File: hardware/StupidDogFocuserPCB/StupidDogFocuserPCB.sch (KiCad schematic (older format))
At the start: 17 parts, among them M1 Stepper_Motor_bipolar, SW1 Rotary_Encoder_Switch, U1 DHT11, U2 SN74HC14N

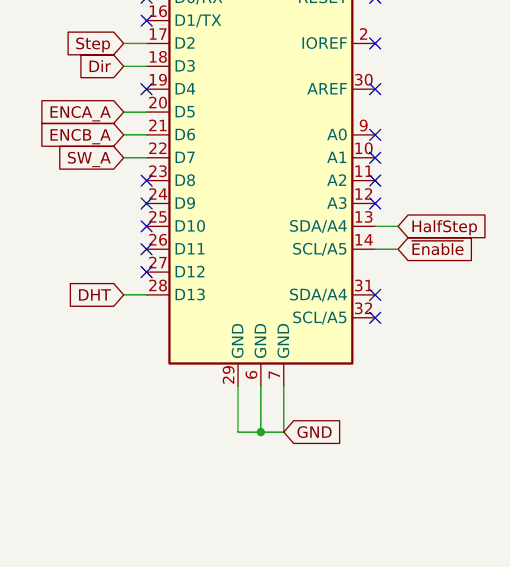
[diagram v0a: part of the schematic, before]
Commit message: moved dht pin.
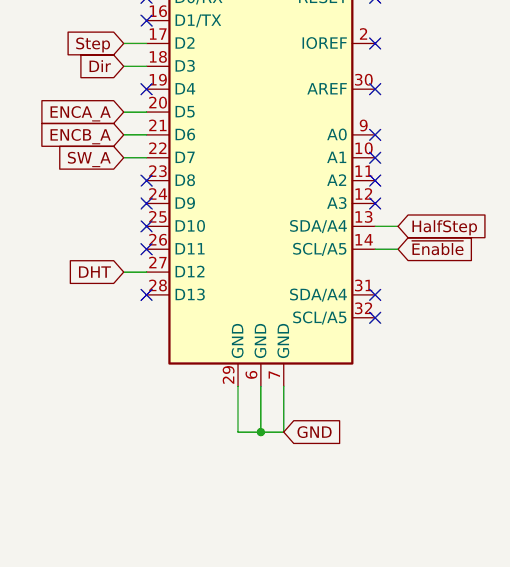
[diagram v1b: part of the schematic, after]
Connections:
- net DHT: now also A2.27 (D12); no longer A2.28 (D13)
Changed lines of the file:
@@
 $EndDescr
-Wire Wire Line
-	2150 3050 2250 3050
 Wire Wire Line
 	3250 2750 3350 2750
@@
 Text GLabel 7650 5700 3    50   Input ~ 0
 DHT
-Text GLabel 2150 3050 0    50   Input ~ 0
+Text GLabel 2150 2950 0    50   Input ~ 0
 DHT
 Text GLabel 3350 2750 2    50   Input ~ 0
@@
 NoConn ~ 3250 3050
 NoConn ~ 3250 3150
-NoConn ~ 2250 2950
 NoConn ~ 2250 2850
 NoConn ~ 2250 2750
@@
 NoConn ~ 5900 2900
 NoConn ~ 5900 1900
+Wire Wire Line
+	2150 2950 2250 2950
+NoConn ~ 2250 3050
 $EndSCHEMATC
